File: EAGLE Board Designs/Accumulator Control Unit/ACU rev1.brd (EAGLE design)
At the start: 186.7 x 135.7 mm, 194 parts, among them J1 CONNECTOR-CAN_MF_T_V_, J2 CONNECTOR-8_MF_T_V_, J3 CONNECTOR-8_MF_T_V_, J4 CONNECTOR-2_MF_T_V_, J5 CONNECTOR-12_MF_T_V_, Q1 TRANSISTOR_N_MOS__PMV15ENEA, Q2 TRANSISTOR_N_MOS__PMV15ENEA, T1 TRANSFORMER_HM2112ZNLT_AIRGAP, U10 OPAMP_1_CHANNEL_OPA991, U11 LOGICGATE_AND_DCK3, U12 OPAMP_1_CHANNEL_OPA991, U13 OPAMP_1_CHANNEL_OPA991, U14 OPAMP_1_CHANNEL_OPA991, U15 LOGICGATE_AND_DCK3, U18 OPAMP_1_CHANNEL_OPA991, U19 MAX7404, U2 ADG1423, U20 OPAMP_1_CHANNEL_OPA991, U22 OPAMP_1_CHANNEL_OPA991, U25 TCAN1051HQV-Q1, U26 MAX7404, U27 OPAMP_1_CHANNEL_OPA991, U28 MAX7404, U29 OPAMP_1_CHANNEL_OPA991, U3 LM555, U30 MAX7404, U4 OPAMP_1_CHANNEL_OPA991, U5 LTC6820, U6 ADM823, U7 OPAMP_1_CHANNEL_OPA991, U8 LOGICGATE_AND_DCK3, U9 OPAMP_1_CHANNEL_OPA991

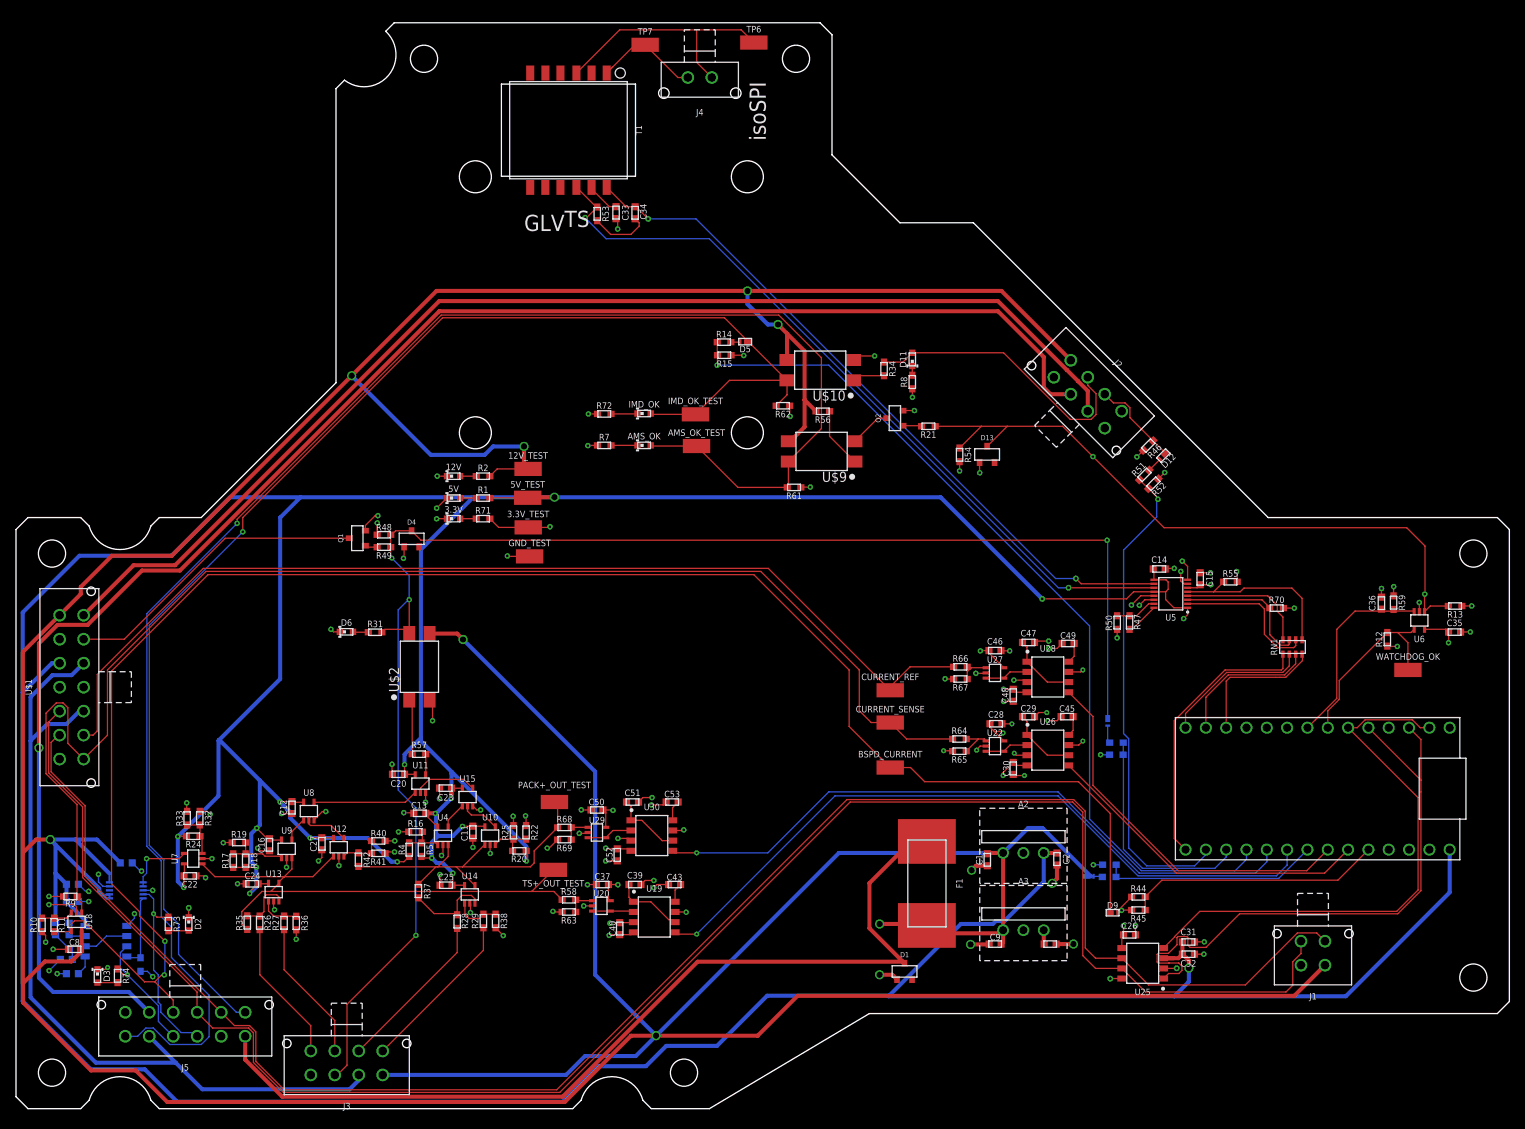
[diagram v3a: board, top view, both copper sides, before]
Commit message: fix hole spacing and add some leds
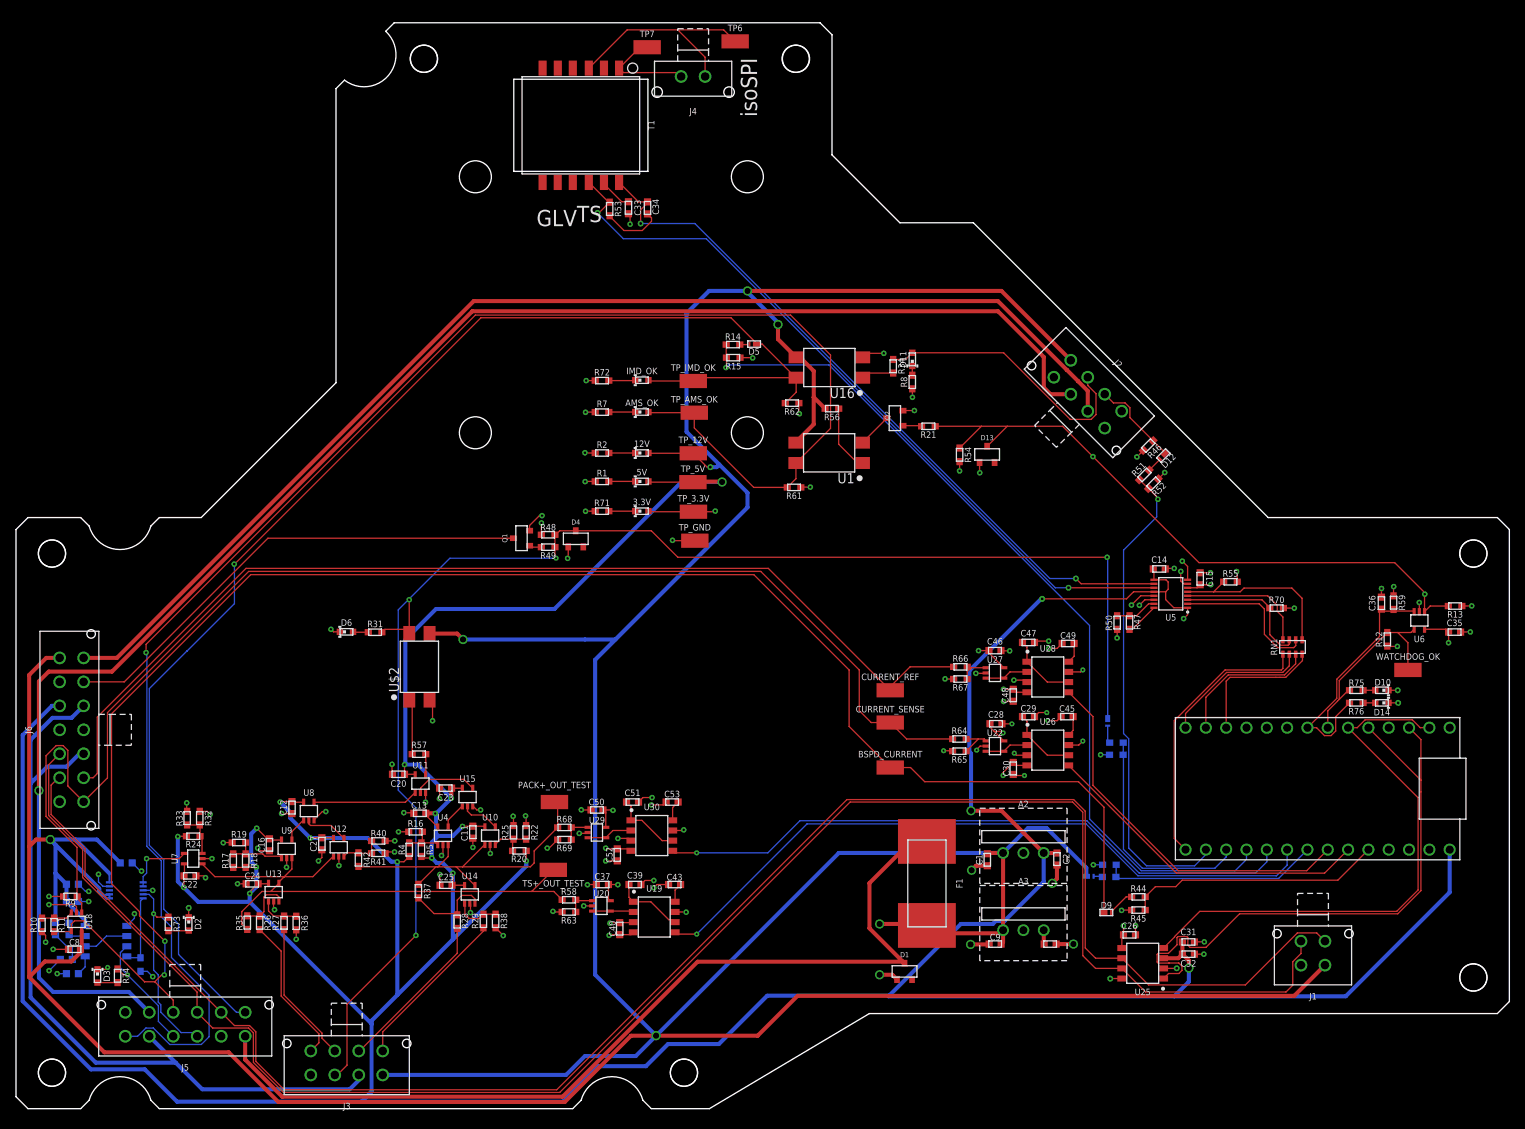
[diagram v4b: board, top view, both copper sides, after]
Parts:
- removed 12V_TEST, 3.3V_TEST, 5V_TEST, AMS_OK_TEST, GND_TEST, IMD_OK_TEST: TEST_POINT, HyTechDevices - Copy:MICRO_MINIATURE
- removed U$1: CONNECTOR-14_MF_T_V_, HyTechDevices - Copy:MOLEX_MICROFIT_PTH_VERTICAL_14_DUAL
- removed U$10, U$9: RELAY_SOLIDSTATE_NO, HyTechDevices:DIP-4
- added D10: LED_0603_GREEN, HyTechDevices:0603-LED
- added D14: LED_0603_RED, HyTechDevices:0603-LED
- added J6: CONNECTOR-14_MF_T_V_, HyTechDevices - Copy:MOLEX_MICROFIT_PTH_VERTICAL_14_DUAL
- added R75, R76: RESISTOR_0603_470, HyTechDevices - Copy:0603-RES
- added TP_12V, TP_3.3V, TP_5V, TP_AMS_OK, TP_GND, TP_IMD_OK: TEST_POINT, HyTechDevices - Copy:MICRO_MINIATURE
- added U$11, U$12, U$13, U$14, U$6, U$7, U$8: (no value), HyTechDevices:MOUNTING_M3
- added U1, U16: RELAY_SOLIDSTATE_NO, HyTechDevices:DIP-4
- moved 12V 23.7 mm to (78.2, 80.5)
- moved 5V 23.6 mm to (78.2, 76.9)
- moved 3.3V 23.6 mm to (78.2, 73.2)
- moved R48 20.5 mm to (66.5, 70.2)
- moved R49 20.5 mm to (66.5, 68.7)
- moved D4 20.5 mm to (70.0, 69.7)
- moved Q1 20.5 mm to (63.2, 69.8)
- moved R2 15.1 mm to (73.3, 80.5)
- moved R1 15.0 mm to (73.3, 76.9)
- moved R71 14.9 mm to (73.3, 73.2)
- moved R72 4.17 mm to (73.3, 89.5)
- moved AMS_OK 4.17 mm to (78.2, 85.6)
- moved IMD_OK 4.17 mm to (78.2, 89.6)
- moved R7 4.17 mm to (73.3, 85.6)
- moved U$4 3.17 mm to (91.6, 126.2)
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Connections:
- new net N$47: D10.2, R75.1
- new net N$59: D14.2, R76.1
- net +12V: now also 12V.2, J6.7, TP_12V.1, U1.4, U16.4; no longer 12V_TEST.1, R2.2, U$1.7, U$10.4, U$9.4
- net +3V3: now also 3.3V.2, TP_3.3V.1; no longer 3.3V_TEST.1, R71.2
- net +5V: now also 5V.2, J6.5, TP_5V.1; no longer 5V_TEST.1, R1.2, U$1.5
- net ACCUMULATOR_GND: now also J6.14; no longer U$1.14
- net AIR2-: now also J6.13; no longer U$1.13
- net AMS_OK: now also TP_AMS_OK.1, U1.3; no longer AMS_OK_TEST.1, U$9.3
- net CANH: now also J6.3; no longer U$1.3
- net CANL: now also J6.2; no longer U$1.2
- net CURRENT: now also J6.8; no longer U$1.8
- net CURRENT_REF: now also J6.9; no longer U$1.9
- net GND: now also D10.1, D14.1, J6.11, J6.4, J6.6, R1.1, R2.1, R71.1, TP_GND.1, U16.2; no longer 12V.1, 3.3V.1, 5V.1, GND_TEST.1, J2.5, U$1.11, U$1.4, U$1.6, U$10.2
- net IMD_OK: now also TP_IMD_OK.1, U16.3; no longer IMD_OK_TEST.1, U$10.3
- net N$1: now also 3.3V.1, R71.2; no longer 12V.2, R2.1
- net N$14: now also 12V.1, R2.2; no longer 3.3V.2, R71.1
- net N$16: now also U1.1; no longer U$9.1
- net N$2: now also 5V.1, R1.2; no longer 5V.2, R1.1
- net N$20: now also U1.2; no longer U$9.2
- net N$8: now also U16.1; no longer U$10.1
- net SHDN: now also J6.10, J6.12; no longer U$1.10, U$1.12
- net TEENSY_OK: now also R76.2
- net WATCHDOG_INPUT: now also R75.2
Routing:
- net +5V: track 685.1 -> 612.0 mm, vias 19 -> 20
- net +12V: track 696.7 -> 628.7 mm, vias 8 -> 7
- net AIR2-: track 38.4 -> 61.2 mm
- net PRECHARGE_OK: track 194.8 -> 187.6 mm
- net TEENSY_OK: track 25.0 -> 31.6 mm
- net CANL: track 225.9 -> 220.6 mm
- net SHDN: track 105.7 -> 100.3 mm
- net CANH: track 230.8 -> 225.5 mm
- net IP: track 31.8 -> 28.1 mm
- net BSPD_CURRENT: track 222.6 -> 219.1 mm
- net AMS_OK_3.3V: track 86.3 -> 82.9 mm
- net CURRENT: track 172.4 -> 169.2 mm
- net PACK+_FILTERED: track 83.9 -> 80.9 mm
- net TS+_OUT_FILTERED: track 90.4 -> 87.5 mm
- net CHASSIS_GND: track 210.1 -> 207.3 mm
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
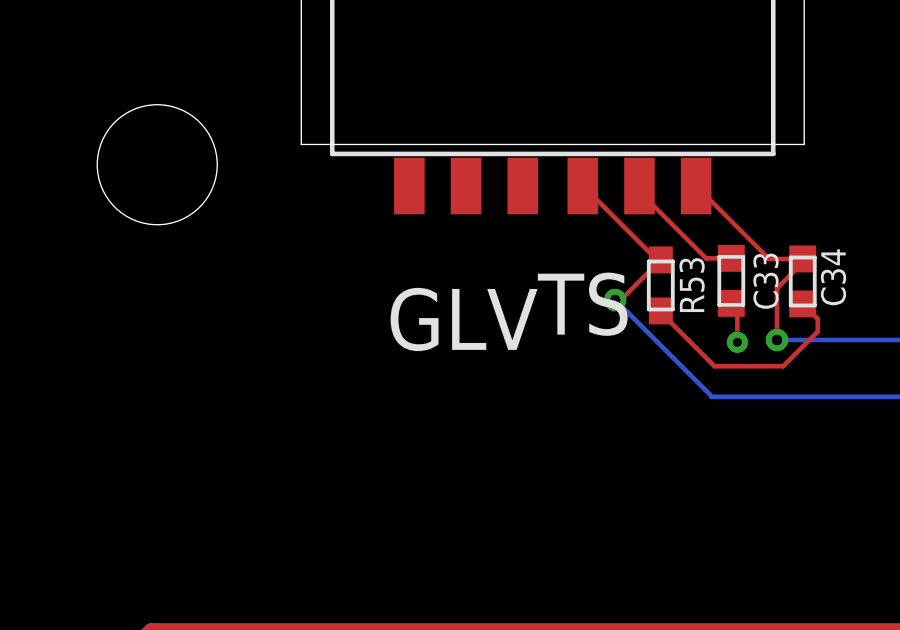
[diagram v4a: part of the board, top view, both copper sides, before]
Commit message: adjust silkscreen
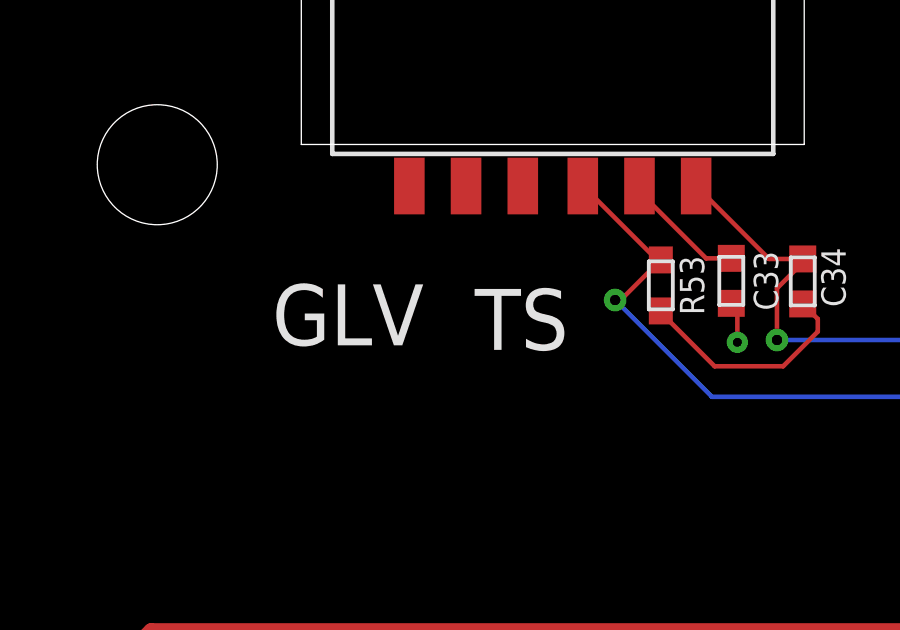
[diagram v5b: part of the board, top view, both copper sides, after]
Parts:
- moved U$5 3.81 mm to (63.8, 110.0)
- moved U$3 2.17 mm to (69.6, 109.8)
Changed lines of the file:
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@@
 <attribute name="VOLTAGE_MAX" value="75V" x="73.2536" y="89.5096" size="1.778" layer="27" display="off"/>
 </element>
-<element name="U$3" library="HyTechAesthetics" package="TS" value="" x="71.6788" y="110.3376" smashed="yes"/>
+<element name="U$3" library="HyTechAesthetics" package="TS" value="" x="69.5706" y="109.8296" smashed="yes"/>
 <element name="U$4" library="HyTechAesthetics" package="ISOSPI" value="" x="91.6178" y="126.1618" smashed="yes" rot="R90"/>
-<element name="U$5" library="HyTechAesthetics" package="GLV" value="" x="67.5894" y="109.8296" smashed="yes" rot="R180"/>
+<element name="U$5" library="HyTechAesthetics" package="GLV" value="" x="63.7794" y="109.982" smashed="yes" rot="R180"/>
 <element name="D2" library="HyTechDevices" package="0603-LED" value="LED_0603_GREEN" x="21.59" y="21.59" smashed="yes" rot="R270">
 <attribute name="COLOR" value="Green" x="21.59" y="21.59" size="1.778" layer="27" rot="R270" display="off"/>

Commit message: post review
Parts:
- removed R55: RESISTOR_0603_10K, HyTechDevices - Copy:0603-RES
- added U$1, U$9: (no value), HyTechAesthetics:TS
- added U$10: (no value), HyTechAesthetics:GLV
- U$4: device HyTechAesthetics:ISOSPI -> HyTechAesthetics:HV_0.50"
- moved U$5 34.7 mm to (98.5, 110.4)
- moved U$3 27.5 mm to (91.6, 126.2), turned to 90 degrees
- moved U$4 9.91 mm to (84.5, 119.2), turned to 0 degrees
- moved T1 5.44 mm to (70.5, 116.0)
- moved C33 5.44 mm to (76.4, 105.7)
- moved C34 5.44 mm to (78.8, 105.7)
- moved R53 5.44 mm to (74.1, 105.5)
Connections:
- net +12V: no longer U$2.4
- net +3V3: no longer R55.2
- net +5V: now also U$2.4
- net CS_LTC_6820: no longer R55.1
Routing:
- net +12V: track 628.7 -> 605.2 mm, vias 7 -> 6
- net IM: track 13.2 -> 19.7 mm
- net +5V: track 612.0 -> 618.1 mm, vias 20 -> 21
- net IP: track 28.1 -> 33.7 mm
- net N$38: track 90.6 -> 88.5 mm
- net N$35: track 94.7 -> 92.6 mm
- net CS_LTC_6820: track 22.0 -> 20.2 mm
- net +3V3: track 58.7 -> 57.4 mm, vias 18 -> 17
- net SHDN: track 100.3 -> 101.1 mm

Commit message: some changes
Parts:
- removed A3: VOLTAGE_REGULATOR_MODULE_OKI-78SR_3.3V, HyTechDevices - Copy:OKI-78SR
- added TP_TSAL_GREEN, TP_TSAL_RED: TEST_POINT, HyTechDevices - Copy:MICRO_MINIATURE
- added U$15: (no value), HyTechAesthetics:LOGO_HYTECH_1.0"
- added U$16: (no value), HyTechAesthetics:LOGO_GT_0.50"
- added U17: VOLTAGE_REGULATOR_SOT223_3.3V, HyTechDevices - Copy:SOT223
- C10: value CAPACITOR_0603_25V_10UF -> CAPACITOR_0603_10V_4.7UF; device HyTechDevices:0603-CAP -> HyTechDevices - Copy:0603-CAP
- C5: value CAPACITOR_0603_10V_4.7NF -> CAPACITOR_0603_10V_4.7UF
- C9: value CAPACITOR_0603_25V_10UF -> CAPACITOR_0603_10V_1UF; device HyTechDevices:0603-CAP -> HyTechDevices - Copy:0603-CAP
- U$1: device HyTechAesthetics:TS -> HyTechAesthetics:GLV
- U$10: device HyTechAesthetics:GLV -> HyTechAesthetics:TS
- moved U$5 45.7 mm to (55.9, 127.0), turned to 90 degrees
- moved U$10 43.6 mm to (97.8, 115.6), turned to 180 degrees
- moved C9 10.1 mm to (132.4, 17.3), turned to 270 degrees
- moved U$1 6.48 mm to (99.1, 109.2)
- moved C10 3.82 mm to (127.0, 16.0), turned to 180 degrees
- moved C33 1.31 mm to (75.2, 105.3)
- moved R53 1.19 mm to (72.9, 105.3)
- moved C1 1.11 mm to (121.2, 28.5)
- moved C34 0.99 mm to (77.9, 105.3)
- moved C5 0.20 mm to (6.15, 17.0)
- turned U$9 to 90 degrees
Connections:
- net +12V: no longer A3.1, C9.1
- net +3V3: now also C14.1, U17.2, U17.4, U5.1, U5.12, U5.9; no longer A3.3
- net +5V: now also C9.1, U17.3; no longer C14.1, U5.1, U5.12, U5.9
- net GND: now also U17.1; no longer A3.2
- net TSAL_GREEN: now also TP_TSAL_GREEN.1
- net TSAL_RED: now also TP_TSAL_RED.1
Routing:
- net +5V: track 618.1 -> 567.0 mm, vias 21 -> 18
- net +3V3: track 57.4 -> 86.1 mm, vias 17 -> 22
- net TSAL_GREEN: track 23.9 -> 38.3 mm
- net +12V: track 605.2 -> 592.0 mm
- net TSAL_RED: track 15.9 -> 26.1 mm
- net CANH: track 225.5 -> 221.2 mm
- net CANL: track 220.6 -> 216.7 mm
- net GND: track 187.4 -> 189.3 mm, vias 122 -> 123
- net N$38: track 88.5 -> 89.6 mm
- net N$35: track 92.6 -> 93.4 mm
